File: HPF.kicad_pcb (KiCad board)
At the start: 4 copper layers, 100 x 100 mm, 827 parts, among them J1 CONN_COAXIAL, J2 Conn_01x12, J3 CONN_COAXIAL, J4 CONN_COAXIAL, J5 CONN_COAXIAL, Q2 zvp2106G, U1 AP1117-50, U2 PGA103+

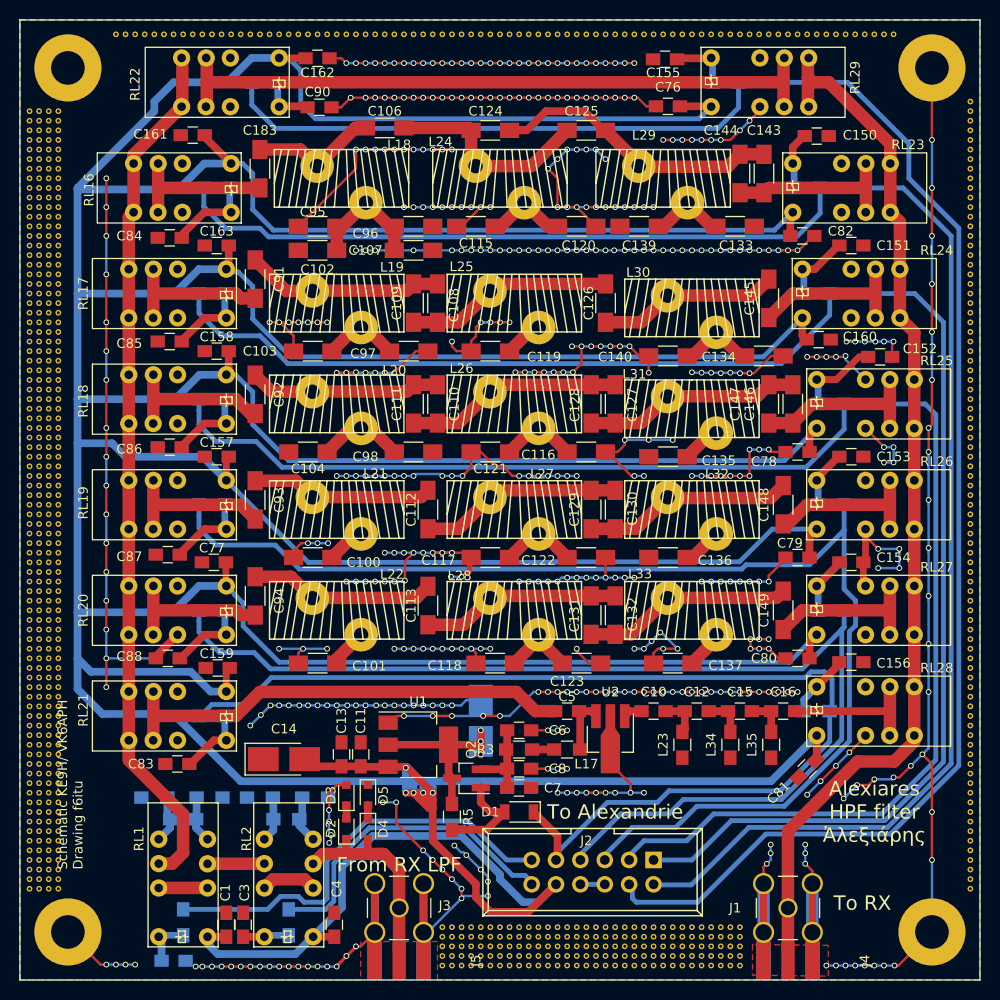
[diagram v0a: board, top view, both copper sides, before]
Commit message: Bad MosFET footprint corrected, new gerber
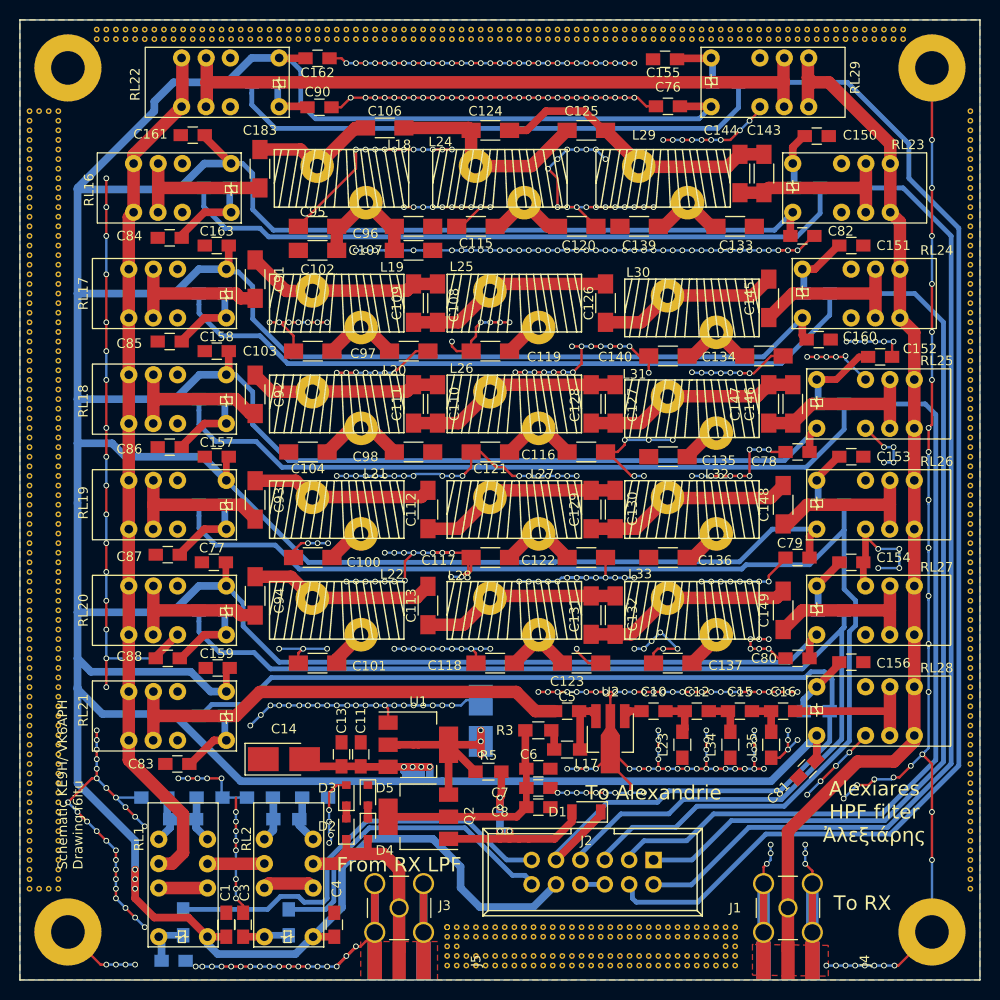
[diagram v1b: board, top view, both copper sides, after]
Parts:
- removed the REF** at (165.0, 111.0)
- removed the REF** at (156.0, 111.0)
- removed the REF** at (162.0, 108.0)
- removed the REF** at (161.0, 108.0)
- removed the REF** at (160.0, 108.0)
- removed the REF** at (159.0, 108.0)
- removed the REF** at (158.0, 108.0)
- removed the REF** at (157.0, 108.0)
- removed the REF** at (156.0, 108.0)
- removed the REF** at (155.0, 108.0)
- removed the REF** at (154.0, 108.0)
- removed the REF** at (153.0, 108.0)
- removed the REF** at (155.0, 111.0)
- removed the REF** at (152.0, 108.0)
- removed the REF** at (151.0, 108.0)
- removed the REF** at (150.0, 108.0)
- removed the REF** at (149.0, 108.0)
- removed the REF** at (148.0, 108.0)
- removed the REF** at (147.0, 108.0)
- removed the REF** at (146.0, 108.0)
- removed the REF** at (145.0, 108.0)
- removed the REF** at (144.0, 108.0)
- removed the REF** at (143.0, 108.0)
- removed the REF** at (154.0, 111.0)
- removed the REF** at (142.0, 108.0)
- removed the REF** at (141.0, 108.0)
- removed the REF** at (140.0, 108.0)
- removed the REF** at (139.0, 108.0)
- removed the REF** at (138.0, 108.0)
- removed the REF** at (137.0, 108.0)
- removed the REF** at (136.0, 108.0)
- removed the REF** at (135.0, 108.0)
- removed the REF** at (134.0, 108.0)
- removed the REF** at (165.0, 107.0)
- removed the REF** at (153.0, 111.0)
- removed the REF** at (164.0, 107.0)
- removed the REF** at (163.0, 107.0)
- removed the REF** at (162.0, 107.0)
- removed the REF** at (161.0, 107.0)
- removed the REF** at (160.0, 107.0)
- removed the REF** at (159.0, 107.0)
- removed the REF** at (158.0, 107.0)
- removed the REF** at (157.0, 107.0)
- removed the REF** at (156.0, 107.0)
- removed the REF** at (155.0, 107.0)
- removed the REF** at (152.0, 111.0)
- removed the REF** at (154.0, 107.0)
- removed the REF** at (153.0, 107.0)
- removed the REF** at (152.0, 107.0)
- removed the REF** at (151.0, 107.0)
- removed the REF** at (150.0, 107.0)
- removed the REF** at (149.0, 107.0)
- removed the REF** at (148.0, 107.0)
- removed the REF** at (147.0, 107.0)
- removed the REF** at (146.0, 107.0)
- removed the REF** at (145.0, 107.0)
- removed the REF** at (151.0, 111.0)
- removed the REF** at (144.0, 107.0)
- removed the REF** at (143.0, 107.0)
- removed the REF** at (142.0, 107.0)
- removed the REF** at (141.0, 107.0)
- removed the REF** at (140.0, 107.0)
- removed the REF** at (139.0, 107.0)
- removed the REF** at (138.0, 107.0)
- removed the REF** at (137.0, 107.0)
- removed the REF** at (136.0, 107.0)
- removed the REF** at (135.0, 107.0)
- removed the REF** at (150.0, 111.0)
- removed the REF** at (134.0, 107.0)
- removed the REF** at (149.0, 111.0)
- removed the REF** at (148.0, 111.0)
- removed the REF** at (147.0, 111.0)
- removed the REF** at (164.0, 111.0)
- removed the REF** at (146.0, 111.0)
- removed the REF** at (145.0, 111.0)
- removed the REF** at (144.0, 111.0)
- removed the REF** at (143.0, 111.0)
- removed the REF** at (142.0, 111.0)
- removed the REF** at (189.0, 21.0)
- removed the REF** at (181.0, 14.0)
- removed the REF** at (180.0, 14.0)
- removed the REF** at (179.0, 14.0)
- removed the REF** at (178.0, 14.0)
- removed the REF** at (177.0, 14.0)
- removed the REF** at (176.0, 14.0)
- removed the REF** at (141.0, 111.0)
- removed the REF** at (175.0, 14.0)
- removed the REF** at (174.0, 14.0)
- removed the REF** at (173.0, 14.0)
- removed the REF** at (172.0, 14.0)
- removed the REF** at (171.0, 14.0)
- removed the REF** at (170.0, 14.0)
- removed the REF** at (169.0, 14.0)
- removed the REF** at (168.0, 14.0)
- removed the REF** at (167.0, 14.0)
- removed the REF** at (166.0, 14.0)
- removed the REF** at (140.0, 111.0)
- removed the REF** at (165.0, 14.0)
- removed the REF** at (164.0, 14.0)
- removed the REF** at (163.0, 14.0)
- removed the REF** at (162.0, 14.0)
- removed the REF** at (161.0, 14.0)
- removed the REF** at (160.0, 14.0)
- removed the REF** at (159.0, 14.0)
- removed the REF** at (158.0, 14.0)
- removed the REF** at (157.0, 14.0)
- removed the REF** at (156.0, 14.0)
- removed the REF** at (139.0, 111.0)
- removed the REF** at (155.0, 14.0)
- removed the REF** at (154.0, 14.0)
- removed the REF** at (153.0, 14.0)
- removed the REF** at (152.0, 14.0)
- removed the REF** at (151.0, 14.0)
- removed the REF** at (150.0, 14.0)
- removed the REF** at (149.0, 14.0)
- removed the REF** at (148.0, 14.0)
- removed the REF** at (147.0, 14.0)
- removed the REF** at (146.0, 14.0)
- removed the REF** at (138.0, 111.0)
- removed the REF** at (145.0, 14.0)
- removed the REF** at (144.0, 14.0)
- removed the REF** at (143.0, 14.0)
- removed the REF** at (142.0, 14.0)
- removed the REF** at (141.0, 14.0)
- removed the REF** at (140.0, 14.0)
- removed the REF** at (139.0, 14.0)
- removed the REF** at (138.0, 14.0)
- removed the REF** at (137.0, 14.0)
- removed the REF** at (136.0, 14.0)
- removed the REF** at (137.0, 111.0)
- removed the REF** at (135.0, 14.0)
- removed the REF** at (134.0, 14.0)
- removed the REF** at (133.0, 14.0)
- removed the REF** at (132.0, 14.0)
- removed the REF** at (131.0, 14.0)
- removed the REF** at (130.0, 14.0)
- removed the REF** at (129.0, 14.0)
- removed the REF** at (128.0, 14.0)
- removed the REF** at (127.0, 14.0)
- removed the REF** at (126.0, 14.0)
- removed the REF** at (163.0, 111.0)
- removed the REF** at (136.0, 111.0)
- removed the REF** at (125.0, 14.0)
- removed the REF** at (124.0, 14.0)
- removed the REF** at (123.0, 14.0)
- removed the REF** at (122.0, 14.0)
- removed the REF** at (121.0, 14.0)
- removed the REF** at (120.0, 14.0)
- removed the REF** at (119.0, 14.0)
- removed the REF** at (118.0, 14.0)
- removed the REF** at (117.0, 14.0)
- removed the REF** at (116.0, 14.0)
- removed the REF** at (135.0, 111.0)
- removed the REF** at (115.0, 14.0)
- removed the REF** at (114.0, 14.0)
- removed the REF** at (113.0, 14.0)
- removed the REF** at (112.0, 14.0)
- removed the REF** at (111.0, 14.0)
- removed the REF** at (110.0, 14.0)
- removed the REF** at (109.0, 14.0)
- removed the REF** at (108.0, 14.0)
- removed the REF** at (107.0, 14.0)
- removed the REF** at (106.0, 14.0)
- removed the REF** at (134.0, 111.0)
- removed the REF** at (105.0, 14.0)
- removed the REF** at (104.0, 14.0)
- removed the REF** at (103.0, 14.0)
- removed the REF** at (102.0, 14.0)
- removed the REF** at (101.0, 14.0)
- removed the REF** at (100.0, 14.0)
- removed the REF** at (165.0, 110.0)
- removed the REF** at (93.0, 102.0)
- removed the REF** at (92.0, 102.0)
- removed the REF** at (93.0, 101.0)
- removed the REF** at (92.0, 101.0)
- removed the REF** at (93.0, 100.0)
- removed the REF** at (164.0, 110.0)
- removed the REF** at (92.0, 100.0)
- removed the REF** at (93.0, 99.0)
- removed the REF** at (92.0, 99.0)
- removed the REF** at (93.0, 98.0)
- removed the REF** at (92.0, 98.0)
- removed the REF** at (163.0, 110.0)
- removed the REF** at (93.0, 97.0)
- removed the REF** at (92.0, 97.0)
- removed the REF** at (93.0, 96.0)
- removed the REF** at (92.0, 96.0)
- removed the REF** at (93.0, 95.0)
- removed the REF** at (162.0, 110.0)
- removed the REF** at (92.0, 95.0)
- removed the REF** at (93.0, 94.0)
- removed the REF** at (92.0, 94.0)
- removed the REF** at (93.0, 93.0)
- removed the REF** at (92.0, 93.0)
- removed the REF** at (161.0, 110.0)
- removed the REF** at (93.0, 92.0)
- removed the REF** at (92.0, 92.0)
- removed the REF** at (93.0, 91.0)
- removed the REF** at (92.0, 91.0)
- removed the REF** at (93.0, 90.0)
- removed the REF** at (160.0, 110.0)
- removed the REF** at (92.0, 90.0)
- removed the REF** at (93.0, 89.0)
- removed the REF** at (92.0, 89.0)
- removed the REF** at (93.0, 88.0)
- removed the REF** at (92.0, 88.0)
- removed the REF** at (159.0, 110.0)
- removed the REF** at (93.0, 87.0)
- removed the REF** at (92.0, 87.0)
- removed the REF** at (93.0, 86.0)
- removed the REF** at (92.0, 86.0)
- removed the REF** at (93.0, 85.0)
- removed the REF** at (162.0, 111.0)
- removed the REF** at (158.0, 110.0)
- removed the REF** at (92.0, 85.0)
- removed the REF** at (93.0, 84.0)
- removed the REF** at (92.0, 84.0)
- removed the REF** at (93.0, 83.0)
- removed the REF** at (92.0, 83.0)
- removed the REF** at (157.0, 110.0)
- removed the REF** at (93.0, 82.0)
- removed the REF** at (92.0, 82.0)
- removed the REF** at (93.0, 81.0)
- removed the REF** at (92.0, 81.0)
- removed the REF** at (93.0, 80.0)
- removed the REF** at (156.0, 110.0)
- removed the REF** at (92.0, 80.0)
- removed the REF** at (93.0, 79.0)
- removed the REF** at (92.0, 79.0)
- removed the REF** at (93.0, 78.0)
- removed the REF** at (92.0, 78.0)
- removed the REF** at (155.0, 110.0)
- removed the REF** at (93.0, 77.0)
- removed the REF** at (92.0, 77.0)
- removed the REF** at (93.0, 76.0)
- removed the REF** at (92.0, 76.0)
- removed the REF** at (93.0, 75.0)
- removed the REF** at (154.0, 110.0)
- removed the REF** at (92.0, 75.0)
- removed the REF** at (93.0, 74.0)
- removed the REF** at (92.0, 74.0)
- removed the REF** at (93.0, 73.0)
- removed the REF** at (92.0, 73.0)
- removed the REF** at (153.0, 110.0)
- removed the REF** at (93.0, 72.0)
- removed the REF** at (92.0, 72.0)
- removed the REF** at (93.0, 71.0)
- removed the REF** at (92.0, 71.0)
- removed the REF** at (93.0, 70.0)
- removed the REF** at (152.0, 110.0)
- removed the REF** at (92.0, 70.0)
- removed the REF** at (93.0, 69.0)
- removed the REF** at (92.0, 69.0)
- removed the REF** at (93.0, 68.0)
- removed the REF** at (92.0, 68.0)
- removed the REF** at (151.0, 110.0)
- removed the REF** at (93.0, 67.0)
- removed the REF** at (92.0, 67.0)
- removed the REF** at (93.0, 66.0)
- removed the REF** at (92.0, 66.0)
- removed the REF** at (93.0, 65.0)
- removed the REF** at (150.0, 110.0)
- removed the REF** at (92.0, 65.0)
- removed the REF** at (93.0, 64.0)
- removed the REF** at (92.0, 64.0)
- removed the REF** at (93.0, 63.0)
- removed the REF** at (92.0, 63.0)
- removed the REF** at (149.0, 110.0)
- removed the REF** at (93.0, 62.0)
- removed the REF** at (92.0, 62.0)
- removed the REF** at (93.0, 61.0)
- removed the REF** at (92.0, 61.0)
- removed the REF** at (93.0, 60.0)
- removed the REF** at (161.0, 111.0)
- removed the REF** at (148.0, 110.0)
- removed the REF** at (92.0, 60.0)
- removed the REF** at (93.0, 59.0)
- removed the REF** at (92.0, 59.0)
- removed the REF** at (93.0, 58.0)
- removed the REF** at (92.0, 58.0)
- removed the REF** at (147.0, 110.0)
- removed the REF** at (93.0, 57.0)
- removed the REF** at (92.0, 57.0)
- removed the REF** at (93.0, 56.0)
- removed the REF** at (92.0, 56.0)
- removed the REF** at (93.0, 55.0)
- removed the REF** at (146.0, 110.0)
- removed the REF** at (92.0, 55.0)
- removed the REF** at (93.0, 54.0)
- removed the REF** at (92.0, 54.0)
- removed the REF** at (93.0, 53.0)
- removed the REF** at (92.0, 53.0)
- removed the REF** at (145.0, 110.0)
- removed the REF** at (93.0, 52.0)
- removed the REF** at (92.0, 52.0)
- removed the REF** at (93.0, 51.0)
- removed the REF** at (92.0, 51.0)
- removed the REF** at (93.0, 50.0)
- removed the REF** at (144.0, 110.0)
- removed the REF** at (92.0, 50.0)
- removed the REF** at (93.0, 49.0)
- removed the REF** at (92.0, 49.0)
- removed the REF** at (93.0, 48.0)
- removed the REF** at (92.0, 48.0)
- removed the REF** at (143.0, 110.0)
- removed the REF** at (93.0, 47.0)
- removed the REF** at (92.0, 47.0)
- removed the REF** at (93.0, 46.0)
- removed the REF** at (92.0, 46.0)
- removed the REF** at (93.0, 45.0)
- removed the REF** at (142.0, 110.0)
- removed the REF** at (92.0, 45.0)
- removed the REF** at (93.0, 44.0)
- removed the REF** at (92.0, 44.0)
- removed the REF** at (93.0, 43.0)
- removed the REF** at (92.0, 43.0)
- removed the REF** at (141.0, 110.0)
- removed the REF** at (93.0, 42.0)
- removed the REF** at (92.0, 42.0)
- removed the REF** at (93.0, 41.0)
- removed the REF** at (92.0, 41.0)
- removed the REF** at (93.0, 40.0)
- removed the REF** at (140.0, 110.0)
- removed the REF** at (92.0, 40.0)
- removed the REF** at (93.0, 39.0)
- removed the REF** at (92.0, 39.0)
- removed the REF** at (93.0, 38.0)
- removed the REF** at (92.0, 38.0)
- removed the REF** at (139.0, 110.0)
- removed the REF** at (93.0, 37.0)
- removed the REF** at (92.0, 37.0)
- removed the REF** at (93.0, 36.0)
- removed the REF** at (92.0, 36.0)
- removed the REF** at (93.0, 35.0)
- removed the REF** at (160.0, 111.0)
- removed the REF** at (138.0, 110.0)
- removed the REF** at (92.0, 35.0)
- removed the REF** at (93.0, 34.0)
- removed the REF** at (92.0, 34.0)
- removed the REF** at (93.0, 33.0)
- removed the REF** at (92.0, 33.0)
- removed the REF** at (137.0, 110.0)
- removed the REF** at (93.0, 32.0)
- removed the REF** at (92.0, 32.0)
- removed the REF** at (93.0, 31.0)
- removed the REF** at (92.0, 31.0)
- removed the REF** at (93.0, 30.0)
- removed the REF** at (136.0, 110.0)
- removed the REF** at (92.0, 30.0)
- removed the REF** at (93.0, 29.0)
- removed the REF** at (92.0, 29.0)
- removed the REF** at (93.0, 28.0)
- removed the REF** at (92.0, 28.0)
- removed the REF** at (135.0, 110.0)
- removed the REF** at (93.0, 27.0)
- removed the REF** at (92.0, 27.0)
- removed the REF** at (93.0, 26.0)
- removed the REF** at (92.0, 26.0)
- removed the REF** at (93.0, 25.0)
- removed the REF** at (134.0, 110.0)
- removed the REF** at (92.0, 25.0)
- removed the REF** at (93.0, 24.0)
- removed the REF** at (92.0, 24.0)
- removed the REF** at (93.0, 23.0)
- removed the REF** at (92.0, 23.0)
- removed the REF** at (165.0, 109.0)
- removed the REF** at (164.0, 109.0)
- removed the REF** at (163.0, 109.0)
- removed the REF** at (162.0, 109.0)
- removed the REF** at (161.0, 109.0)
- removed the REF** at (159.0, 111.0)
- removed the REF** at (160.0, 109.0)
- removed the REF** at (159.0, 109.0)
- removed the REF** at (158.0, 109.0)
- removed the REF** at (157.0, 109.0)
- removed the REF** at (156.0, 109.0)
- removed the REF** at (155.0, 109.0)
- removed the REF** at (154.0, 109.0)
- removed the REF** at (153.0, 109.0)
- removed the REF** at (152.0, 109.0)
- removed the REF** at (151.0, 109.0)
- removed the REF** at (158.0, 111.0)
- removed the REF** at (150.0, 109.0)
- removed the REF** at (149.0, 109.0)
- removed the REF** at (148.0, 109.0)
- removed the REF** at (147.0, 109.0)
- removed the REF** at (146.0, 109.0)
- removed the REF** at (145.0, 109.0)
- removed the REF** at (144.0, 109.0)
- removed the REF** at (143.0, 109.0)
- removed the REF** at (142.0, 109.0)
- removed the REF** at (141.0, 109.0)
- removed the REF** at (157.0, 111.0)
- removed the REF** at (140.0, 109.0)
- removed the REF** at (139.0, 109.0)
- removed the REF** at (138.0, 109.0)
- removed the REF** at (137.0, 109.0)
- removed the REF** at (136.0, 109.0)
- removed the REF** at (135.0, 109.0)
- removed the REF** at (134.0, 109.0)
- removed the REF** at (165.0, 108.0)
- removed the REF** at (164.0, 108.0)
- removed the REF** at (163.0, 108.0)
- added REF**: via, via:via, F.Cu at (164.5, 111.0)
- added REF**: via, via:via, F.Cu at (155.5, 111.0)
- added REF**: via, via:via, F.Cu at (162.5, 107.0)
- added REF**: via, via:via, F.Cu at (161.5, 107.0)
- added REF**: via, via:via, F.Cu at (160.5, 107.0)
- added REF**: via, via:via, F.Cu at (159.5, 107.0)
- added REF**: via, via:via, F.Cu at (158.5, 107.0)
- added REF**: via, via:via, F.Cu at (157.5, 107.0)
- added REF**: via, via:via, F.Cu at (156.5, 107.0)
- added REF**: via, via:via, F.Cu at (155.5, 107.0)
- added REF**: via, via:via, F.Cu at (154.5, 107.0)
- added REF**: via, via:via, F.Cu at (153.5, 107.0)
- added REF**: via, via:via, F.Cu at (154.5, 111.0)
- added REF**: via, via:via, F.Cu at (152.5, 107.0)
- added REF**: via, via:via, F.Cu at (151.5, 107.0)
- added REF**: via, via:via, F.Cu at (150.5, 107.0)
- added REF**: via, via:via, F.Cu at (149.5, 107.0)
- added REF**: via, via:via, F.Cu at (148.5, 107.0)
- added REF**: via, via:via, F.Cu at (147.5, 107.0)
- added REF**: via, via:via, F.Cu at (146.5, 107.0)
- added REF**: via, via:via, F.Cu at (145.5, 107.0)
- added REF**: via, via:via, F.Cu at (144.5, 107.0)
- added REF**: via, via:via, F.Cu at (143.5, 107.0)
- added REF**: via, via:via, F.Cu at (153.5, 111.0)
- added REF**: via, via:via, F.Cu at (142.5, 107.0)
- added REF**: via, via:via, F.Cu at (141.5, 107.0)
- added REF**: via, via:via, F.Cu at (140.5, 107.0)
- added REF**: via, via:via, F.Cu at (139.5, 107.0)
- added REF**: via, via:via, F.Cu at (138.5, 107.0)
- added REF**: via, via:via, F.Cu at (137.5, 107.0)
- added REF**: via, via:via, F.Cu at (136.5, 107.0)
- added REF**: via, via:via, F.Cu at (135.5, 107.0)
- added REF** (x2): via, via:via, F.Cu at (134.5, 107.0)
- added REF**: via, via:via, F.Cu at (152.5, 111.0)
- added REF**: via, via:via, F.Cu at (151.5, 111.0)
- added REF**: via, via:via, F.Cu at (150.5, 111.0)
- added REF**: via, via:via, F.Cu at (149.5, 111.0)
- added REF**: via, via:via, F.Cu at (148.5, 111.0)
- added REF**: via, via:via, F.Cu at (147.5, 111.0)
- added REF**: via, via:via, F.Cu at (146.5, 111.0)
- added REF**: via, via:via, F.Cu at (163.5, 111.0)
- added REF**: via, via:via, F.Cu at (145.5, 111.0)
- added REF**: via, via:via, F.Cu at (144.5, 111.0)
- added REF**: via, via:via, F.Cu at (143.5, 111.0)
- added REF**: via, via:via, F.Cu at (142.5, 111.0)
- added REF**: via, via:via, F.Cu at (141.5, 111.0)
- added REF**: via, via:via, F.Cu at (140.5, 111.0)
- added REF**: via, via:via, F.Cu at (139.5, 111.0)
- added REF**: via, via:via, F.Cu at (138.5, 111.0)
- added REF**: via, via:via, F.Cu at (137.5, 111.0)
- added REF**: via, via:via, F.Cu at (136.5, 111.0)
- added REF**: via, via:via, F.Cu at (162.5, 111.0)
- added REF**: via, via:via, F.Cu at (135.5, 111.0)
- added REF**: via, via:via, F.Cu at (134.5, 111.0)
- added REF**: via, via:via, F.Cu at (164.5, 110.0)
- added REF**: via, via:via, F.Cu at (163.5, 110.0)
- added REF**: via, via:via, F.Cu at (162.5, 110.0)
- added REF**: via, via:via, F.Cu at (161.5, 110.0)
- added REF**: via, via:via, F.Cu at (160.5, 110.0)
- added REF**: via, via:via, F.Cu at (159.5, 110.0)
- added REF**: via, via:via, F.Cu at (158.5, 110.0)
- added REF**: via, via:via, F.Cu at (182.0, 14.5)
- added REF**: via, via:via, F.Cu at (181.0, 14.5)
- added REF**: via, via:via, F.Cu at (180.0, 14.5)
- added REF**: via, via:via, F.Cu at (179.0, 14.5)
- added REF**: via, via:via, F.Cu at (178.0, 14.5)
- added REF**: via, via:via, F.Cu at (177.0, 14.5)
- added REF**: via, via:via, F.Cu at (176.0, 14.5)
- added REF**: via, via:via, F.Cu at (175.0, 14.5)
- added REF**: via, via:via, F.Cu at (174.0, 14.5)
- added REF**: via, via:via, F.Cu at (173.0, 14.5)
- added REF**: via, via:via, F.Cu at (157.5, 110.0)
- added REF**: via, via:via, F.Cu at (172.0, 14.5)
- added REF**: via, via:via, F.Cu at (171.0, 14.5)
- added REF**: via, via:via, F.Cu at (170.0, 14.5)
- added REF**: via, via:via, F.Cu at (169.0, 14.5)
- added REF**: via, via:via, F.Cu at (168.0, 14.5)
- added REF**: via, via:via, F.Cu at (167.0, 14.5)
- added REF**: via, via:via, F.Cu at (166.0, 14.5)
- added REF**: via, via:via, F.Cu at (165.0, 14.5)
- added REF**: via, via:via, F.Cu at (164.0, 14.5)
- added REF**: via, via:via, F.Cu at (163.0, 14.5)
- added REF**: via, via:via, F.Cu at (161.5, 111.0)
- added REF**: via, via:via, F.Cu at (156.5, 110.0)
- added REF**: via, via:via, F.Cu at (162.0, 14.5)
- added REF**: via, via:via, F.Cu at (161.0, 14.5)
- added REF**: via, via:via, F.Cu at (160.0, 14.5)
- added REF**: via, via:via, F.Cu at (159.0, 14.5)
- added REF**: via, via:via, F.Cu at (158.0, 14.5)
- added REF**: via, via:via, F.Cu at (157.0, 14.5)
- added REF**: via, via:via, F.Cu at (156.0, 14.5)
- added REF**: via, via:via, F.Cu at (155.0, 14.5)
- added REF**: via, via:via, F.Cu at (154.0, 14.5)
- added REF**: via, via:via, F.Cu at (153.0, 14.5)
- added REF**: via, via:via, F.Cu at (155.5, 110.0)
- added REF**: via, via:via, F.Cu at (152.0, 14.5)
- added REF**: via, via:via, F.Cu at (151.0, 14.5)
- added REF**: via, via:via, F.Cu at (150.0, 14.5)
- added REF**: via, via:via, F.Cu at (149.0, 14.5)
- added REF**: via, via:via, F.Cu at (148.0, 14.5)
- added REF**: via, via:via, F.Cu at (147.0, 14.5)
- added REF**: via, via:via, F.Cu at (146.0, 14.5)
- added REF**: via, via:via, F.Cu at (145.0, 14.5)
- added REF**: via, via:via, F.Cu at (144.0, 14.5)
- added REF**: via, via:via, F.Cu at (143.0, 14.5)
- added REF**: via, via:via, F.Cu at (154.5, 110.0)
- added REF**: via, via:via, F.Cu at (142.0, 14.5)
- added REF**: via, via:via, F.Cu at (141.0, 14.5)
- added REF**: via, via:via, F.Cu at (140.0, 14.5)
- added REF**: via, via:via, F.Cu at (139.0, 14.5)
- added REF**: via, via:via, F.Cu at (138.0, 14.5)
- added REF**: via, via:via, F.Cu at (137.0, 14.5)
- added REF**: via, via:via, F.Cu at (136.0, 14.5)
- added REF**: via, via:via, F.Cu at (135.0, 14.5)
- added REF**: via, via:via, F.Cu at (134.0, 14.5)
- added REF**: via, via:via, F.Cu at (133.0, 14.5)
- added REF**: via, via:via, F.Cu at (153.5, 110.0)
- added REF**: via, via:via, F.Cu at (132.0, 14.5)
- added REF**: via, via:via, F.Cu at (131.0, 14.5)
- added REF**: via, via:via, F.Cu at (130.0, 14.5)
- added REF**: via, via:via, F.Cu at (129.0, 14.5)
- added REF**: via, via:via, F.Cu at (128.0, 14.5)
- added REF**: via, via:via, F.Cu at (127.0, 14.5)
- added REF**: via, via:via, F.Cu at (126.0, 14.5)
- added REF**: via, via:via, F.Cu at (125.0, 14.5)
- added REF**: via, via:via, F.Cu at (124.0, 14.5)
- added REF**: via, via:via, F.Cu at (123.0, 14.5)
- added REF**: via, via:via, F.Cu at (152.5, 110.0)
- added REF**: via, via:via, F.Cu at (122.0, 14.5)
- added REF**: via, via:via, F.Cu at (121.0, 14.5)
- added REF**: via, via:via, F.Cu at (120.0, 14.5)
- added REF**: via, via:via, F.Cu at (119.0, 14.5)
- added REF**: via, via:via, F.Cu at (118.0, 14.5)
- added REF**: via, via:via, F.Cu at (117.0, 14.5)
- added REF**: via, via:via, F.Cu at (116.0, 14.5)
- added REF**: via, via:via, F.Cu at (115.0, 14.5)
- added REF**: via, via:via, F.Cu at (114.0, 14.5)
- added REF**: via, via:via, F.Cu at (113.0, 14.5)
- added REF**: via, via:via, F.Cu at (151.5, 110.0)
- added REF**: via, via:via, F.Cu at (112.0, 14.5)
- added REF**: via, via:via, F.Cu at (111.0, 14.5)
- added REF**: via, via:via, F.Cu at (110.0, 14.5)
- added REF**: via, via:via, F.Cu at (109.0, 14.5)
- added REF**: via, via:via, F.Cu at (108.0, 14.5)
- added REF**: via, via:via, F.Cu at (107.0, 14.5)
- added REF**: via, via:via, F.Cu at (106.0, 14.5)
- added REF**: via, via:via, F.Cu at (105.0, 14.5)
- added REF**: via, via:via, F.Cu at (104.0, 14.5)
- added REF**: via, via:via, F.Cu at (103.0, 14.5)
- added REF**: via, via:via, F.Cu at (150.5, 110.0)
- added REF**: via, via:via, F.Cu at (102.0, 14.5)
- added REF**: via, via:via, F.Cu at (101.0, 14.5)
- added REF**: via, via:via, F.Cu at (100.0, 14.5)
- added REF**: via, via:via, F.Cu at (99.0, 14.5)
- added REF**: via, via:via, F.Cu at (98.0, 14.5)
- added REF**: via, via:via, F.Cu at (182.0, 13.5)
- added REF**: via, via:via, F.Cu at (181.0, 13.5)
- added REF**: via, via:via, F.Cu at (180.0, 13.5)
- added REF**: via, via:via, F.Cu at (179.0, 13.5)
- added REF**: via, via:via, F.Cu at (178.0, 13.5)
- added REF**: via, via:via, F.Cu at (149.5, 110.0)
- added REF**: via, via:via, F.Cu at (177.0, 13.5)
- added REF**: via, via:via, F.Cu at (176.0, 13.5)
- added REF**: via, via:via, F.Cu at (175.0, 13.5)
- added REF**: via, via:via, F.Cu at (174.0, 13.5)
- added REF**: via, via:via, F.Cu at (173.0, 13.5)
- added REF**: via, via:via, F.Cu at (172.0, 13.5)
- added REF**: via, via:via, F.Cu at (171.0, 13.5)
- added REF**: via, via:via, F.Cu at (170.0, 13.5)
- added REF**: via, via:via, F.Cu at (169.0, 13.5)
- added REF**: via, via:via, F.Cu at (168.0, 13.5)
- added REF**: via, via:via, F.Cu at (148.5, 110.0)
- added REF**: via, via:via, F.Cu at (167.0, 13.5)
- added REF**: via, via:via, F.Cu at (166.0, 13.5)
- added REF**: via, via:via, F.Cu at (165.0, 13.5)
- added REF**: via, via:via, F.Cu at (164.0, 13.5)
- added REF**: via, via:via, F.Cu at (163.0, 13.5)
- added REF**: via, via:via, F.Cu at (162.0, 13.5)
- added REF**: via, via:via, F.Cu at (161.0, 13.5)
- added REF**: via, via:via, F.Cu at (160.0, 13.5)
- added REF**: via, via:via, F.Cu at (159.0, 13.5)
- added REF**: via, via:via, F.Cu at (158.0, 13.5)
- added REF**: via, via:via, F.Cu at (147.5, 110.0)
- added REF**: via, via:via, F.Cu at (157.0, 13.5)
- added REF**: via, via:via, F.Cu at (156.0, 13.5)
- added REF**: via, via:via, F.Cu at (155.0, 13.5)
- added REF**: via, via:via, F.Cu at (154.0, 13.5)
- added REF**: via, via:via, F.Cu at (153.0, 13.5)
- added REF**: via, via:via, F.Cu at (152.0, 13.5)
- added REF**: via, via:via, F.Cu at (151.0, 13.5)
- added REF**: via, via:via, F.Cu at (150.0, 13.5)
- added REF**: via, via:via, F.Cu at (149.0, 13.5)
- added REF**: via, via:via, F.Cu at (148.0, 13.5)
- added REF**: via, via:via, F.Cu at (160.5, 111.0)
- added REF**: via, via:via, F.Cu at (146.5, 110.0)
- added REF**: via, via:via, F.Cu at (147.0, 13.5)
- added REF**: via, via:via, F.Cu at (146.0, 13.5)
- added REF**: via, via:via, F.Cu at (145.0, 13.5)
- added REF**: via, via:via, F.Cu at (144.0, 13.5)
- added REF**: via, via:via, F.Cu at (143.0, 13.5)
- added REF**: via, via:via, F.Cu at (142.0, 13.5)
- added REF**: via, via:via, F.Cu at (141.0, 13.5)
- added REF**: via, via:via, F.Cu at (140.0, 13.5)
- added REF**: via, via:via, F.Cu at (139.0, 13.5)
- added REF**: via, via:via, F.Cu at (138.0, 13.5)
- added REF**: via, via:via, F.Cu at (145.5, 110.0)
- added REF**: via, via:via, F.Cu at (137.0, 13.5)
- added REF**: via, via:via, F.Cu at (136.0, 13.5)
- added REF**: via, via:via, F.Cu at (135.0, 13.5)
- added REF**: via, via:via, F.Cu at (134.0, 13.5)
- added REF**: via, via:via, F.Cu at (133.0, 13.5)
- added REF**: via, via:via, F.Cu at (132.0, 13.5)
- added REF**: via, via:via, F.Cu at (131.0, 13.5)
- added REF**: via, via:via, F.Cu at (130.0, 13.5)
- added REF**: via, via:via, F.Cu at (129.0, 13.5)
- added REF**: via, via:via, F.Cu at (128.0, 13.5)
- added REF**: via, via:via, F.Cu at (144.5, 110.0)
- added REF**: via, via:via, F.Cu at (127.0, 13.5)
- added REF**: via, via:via, F.Cu at (126.0, 13.5)
- added REF**: via, via:via, F.Cu at (125.0, 13.5)
- added REF**: via, via:via, F.Cu at (124.0, 13.5)
- added REF**: via, via:via, F.Cu at (123.0, 13.5)
- added REF**: via, via:via, F.Cu at (122.0, 13.5)
- added REF**: via, via:via, F.Cu at (121.0, 13.5)
- added REF**: via, via:via, F.Cu at (120.0, 13.5)
- added REF**: via, via:via, F.Cu at (119.0, 13.5)
- added REF**: via, via:via, F.Cu at (118.0, 13.5)
- added REF**: via, via:via, F.Cu at (143.5, 110.0)
- added REF**: via, via:via, F.Cu at (117.0, 13.5)
- added REF**: via, via:via, F.Cu at (116.0, 13.5)
- added REF**: via, via:via, F.Cu at (115.0, 13.5)
- added REF**: via, via:via, F.Cu at (114.0, 13.5)
- added REF**: via, via:via, F.Cu at (113.0, 13.5)
- added REF**: via, via:via, F.Cu at (112.0, 13.5)
- added REF**: via, via:via, F.Cu at (111.0, 13.5)
- added REF**: via, via:via, F.Cu at (110.0, 13.5)
- added REF**: via, via:via, F.Cu at (109.0, 13.5)
- added REF**: via, via:via, F.Cu at (108.0, 13.5)
- added REF**: via, via:via, F.Cu at (142.5, 110.0)
- added REF**: via, via:via, F.Cu at (107.0, 13.5)
- added REF**: via, via:via, F.Cu at (106.0, 13.5)
- added REF**: via, via:via, F.Cu at (105.0, 13.5)
- added REF**: via, via:via, F.Cu at (104.0, 13.5)
- added REF**: via, via:via, F.Cu at (103.0, 13.5)
- added REF**: via, via:via, F.Cu at (102.0, 13.5)
- added REF**: via, via:via, F.Cu at (101.0, 13.5)
- added REF**: via, via:via, F.Cu at (100.0, 13.5)
- added REF**: via, via:via, F.Cu at (99.0, 13.5)
- added REF**: via, via:via, F.Cu at (98.0, 13.5)
- added REF**: via, via:via, F.Cu at (141.5, 110.0)
- added REF**: via, via:via, F.Cu at (140.5, 110.0)
- added REF**: via, via:via, F.Cu at (139.5, 110.0)
- added REF**: via, via:via, F.Cu at (138.5, 110.0)
- added REF**: via, via:via, F.Cu at (137.5, 110.0)
- added REF**: via, via:via, F.Cu at (159.5, 111.0)
- added REF**: via, via:via, F.Cu at (136.5, 110.0)
- added REF**: via, via:via, F.Cu at (135.5, 110.0)
- added REF**: via, via:via, F.Cu at (134.5, 110.0)
- added REF**: via, via:via, F.Cu at (164.5, 109.0)
- added REF**: via, via:via, F.Cu at (163.5, 109.0)
- added REF**: via, via:via, F.Cu at (135.5, 109.0)
- added REF**: via, via:via, F.Cu at (134.5, 109.0)
- added REF**: via, via:via, F.Cu at (164.5, 108.0)
- added REF**: via, via:via, F.Cu at (163.5, 108.0)
- added REF**: via, via:via, F.Cu at (162.5, 108.0)
- added REF**: via, via:via, F.Cu at (158.5, 111.0)
- added REF**: via, via:via, F.Cu at (161.5, 108.0)
- added REF**: via, via:via, F.Cu at (160.5, 108.0)
- added REF**: via, via:via, F.Cu at (159.5, 108.0)
- added REF**: via, via:via, F.Cu at (158.5, 108.0)
- added REF**: via, via:via, F.Cu at (157.5, 108.0)
- added REF**: via, via:via, F.Cu at (156.5, 108.0)
- added REF**: via, via:via, F.Cu at (155.5, 108.0)
- added REF**: via, via:via, F.Cu at (154.5, 108.0)
- added REF**: via, via:via, F.Cu at (153.5, 108.0)
- added REF**: via, via:via, F.Cu at (152.5, 108.0)
- added REF**: via, via:via, F.Cu at (157.5, 111.0)
- added REF**: via, via:via, F.Cu at (151.5, 108.0)
- added REF**: via, via:via, F.Cu at (150.5, 108.0)
- added REF**: via, via:via, F.Cu at (149.5, 108.0)
- added REF**: via, via:via, F.Cu at (148.5, 108.0)
- added REF**: via, via:via, F.Cu at (147.5, 108.0)
- added REF**: via, via:via, F.Cu at (146.5, 108.0)
- added REF**: via, via:via, F.Cu at (145.5, 108.0)
- added REF**: via, via:via, F.Cu at (144.5, 108.0)
- added REF**: via, via:via, F.Cu at (143.5, 108.0)
- added REF**: via, via:via, F.Cu at (142.5, 108.0)
- added REF**: via, via:via, F.Cu at (156.5, 111.0)
- added REF**: via, via:via, F.Cu at (141.5, 108.0)
- added REF**: via, via:via, F.Cu at (140.5, 108.0)
- added REF**: via, via:via, F.Cu at (139.5, 108.0)
- added REF**: via, via:via, F.Cu at (138.5, 108.0)
- added REF**: via, via:via, F.Cu at (137.5, 108.0)
- added REF**: via, via:via, F.Cu at (136.5, 108.0)
- added REF**: via, via:via, F.Cu at (135.5, 108.0)
- added REF**: via, via:via, F.Cu at (134.5, 108.0)
- added REF**: via, via:via, F.Cu at (164.5, 107.0)
- added REF**: via, via:via, F.Cu at (163.5, 107.0)
- C134: value 680 -> 680p
- Q2: footprint TO_SOT_Packages_SMD:SOT-23_Handsoldering -> TO_SOT_Packages_SMD:SOT-223-3Lead_TabPin2
- R1, R2: value R -> 100R
- R10: value R -> 75R
- R11: value R -> 240R
- R12, R13: value R -> 62R
- moved D1 7.00 mm to (149.0, 95.0)
- moved Q2 6.40 mm to (131.5, 95.5)
- moved R5 6.04 mm to (138.8, 90.8), turned to 0 degrees
- moved C6 4.47 mm to (144.0, 90.5)
- moved C8 4.47 mm to (144.0, 94.5)
- moved R3 2.83 mm to (144.0, 86.5)
- moved C7 2.00 mm to (144.0, 92.5)
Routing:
- net GND: track 857.0 -> 905.8 mm, vias 477 -> 526
- net Net-(C6-Pad1): track 8.77 -> 22.9 mm
- net Net-(D1-Pad2): track 10.7 -> 24.5 mm, vias 0 -> 4
- net +12V: track 791.4 -> 797.0 mm, vias 5 -> 7
- net Net-(C9-Pad2): track 21.1 -> 26.2 mm
- net 6mLNA: track 114.8 -> 115.7 mm

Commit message: Bad MosFET footprint corrected, new gerber
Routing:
- net GND: track 905.8 -> 936.7 mm, vias 526 -> 609
- net Net-(C143-Pad1): track 18.4 -> 25.4 mm, vias 0 -> 6
